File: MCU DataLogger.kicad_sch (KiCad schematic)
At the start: 25 parts, among them U1 24LC1025, U2 24LC1025, U3 DS1337S+, U4 ATMEGA328P-AU, Y1 32.768 KHz, Y2 16 MHz

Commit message: Completed comments.
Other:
- note added: "EEPROM"
- note added: "MCU"
- note added: "Mounting"
- note added: "Real time clock"
- moved on the sheet: H1, H2, H3, H4

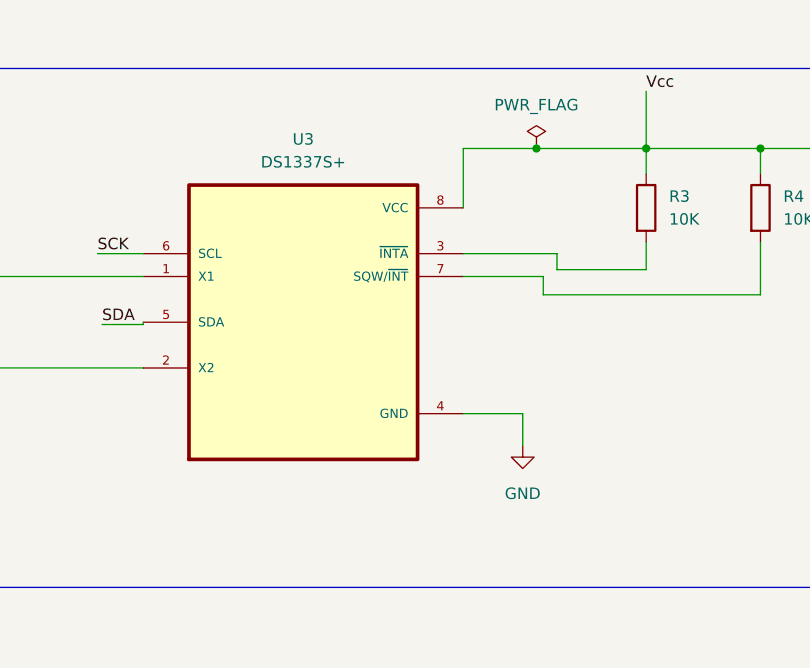
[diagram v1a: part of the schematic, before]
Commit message: First routes.
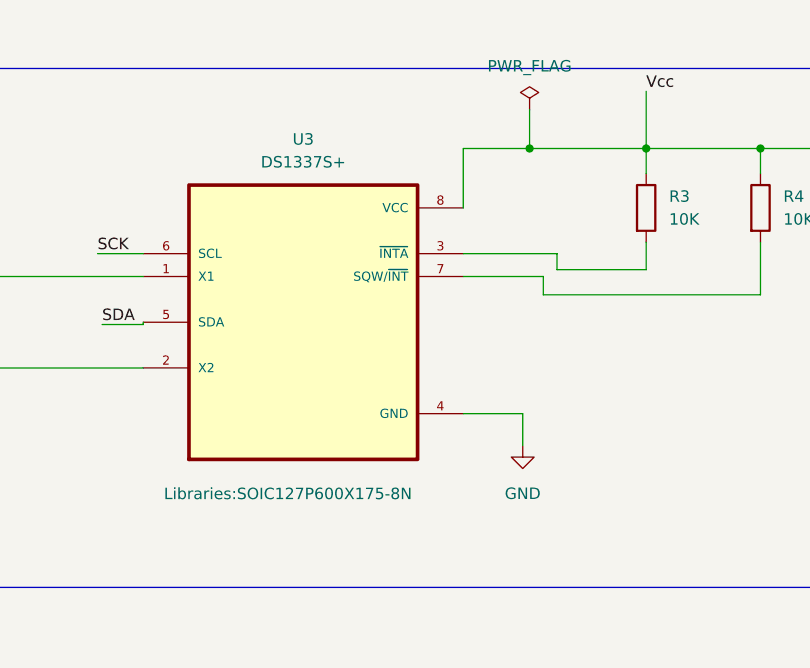
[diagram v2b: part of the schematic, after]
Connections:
- net Vcc: now also C1.1, R3.1, R4.1, U3.8 (VCC)

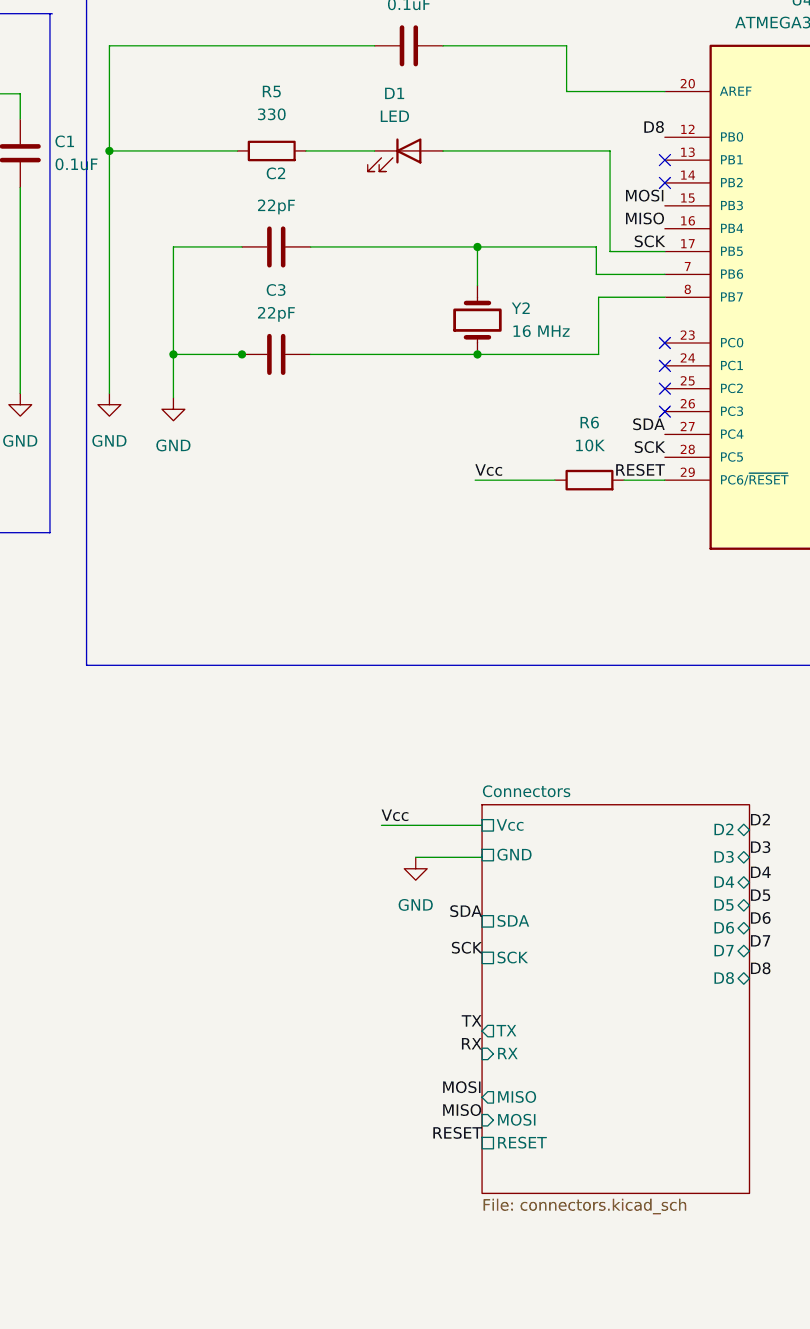
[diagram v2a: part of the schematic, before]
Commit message: Routing sans GND Vcc complete.
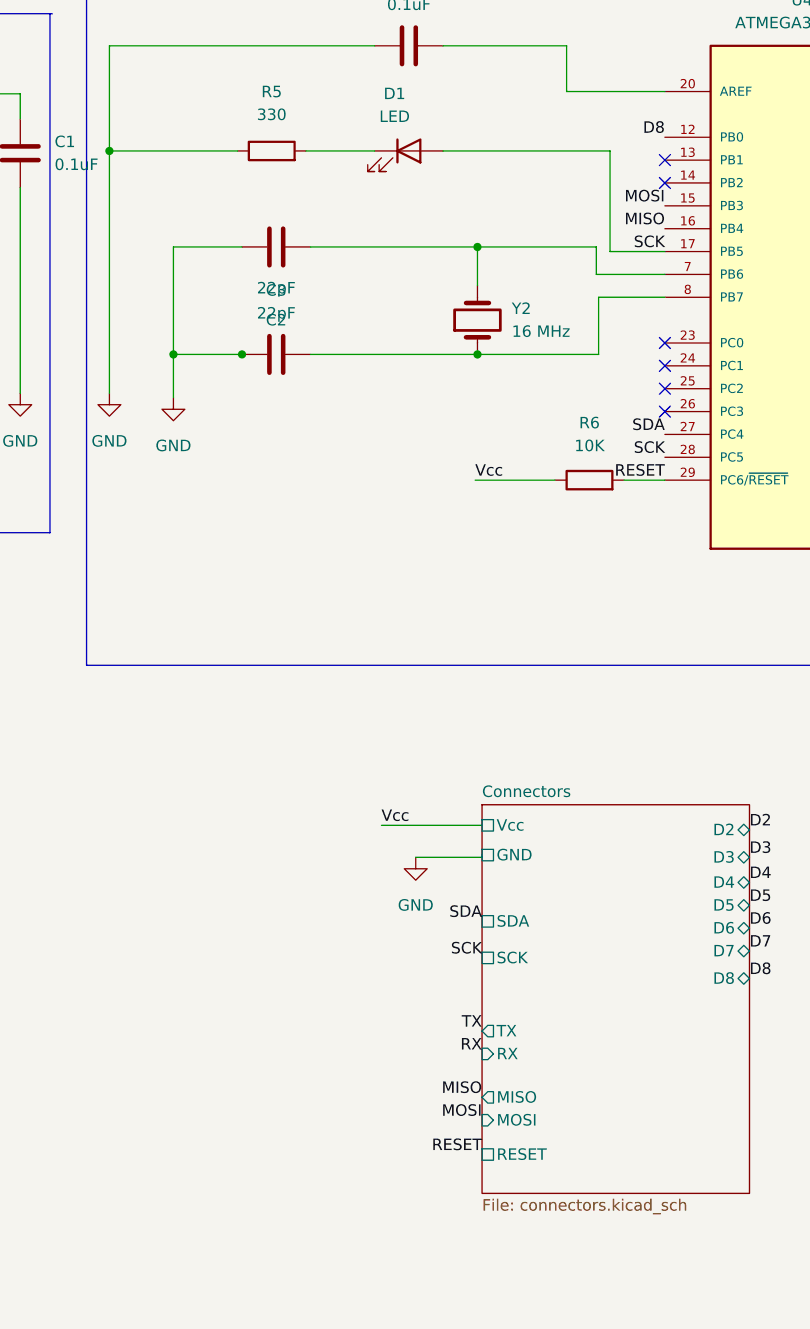
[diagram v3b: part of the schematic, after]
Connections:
- net GND: now also C2.1; no longer C2.2
- net at U4.7 (PB6), Y2.2: now also C2.2; no longer C2.1
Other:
- moved on the sheet: C2
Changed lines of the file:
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@@
     (effects (font (size 1.27 1.27)) (justify left bottom))
   )
-  (label "MISO" (at 183.388 143.002 180)
+  (label "MISO" (at 183.388 140.462 180)
     (effects (font (size 1.27 1.27)) (justify right bottom))
   )
@@
     (effects (font (size 1.27 1.27)) (justify left bottom))
   )
-  (label "RESET" (at 183.388 145.542 180)
+  (label "RESET" (at 183.388 146.812 180)
     (effects (font (size 1.27 1.27)) (justify right bottom))
   )
@@
     (effects (font (size 1.27 1.27)) (justify right bottom))
   )
-  (label "MOSI" (at 183.388 140.462 180)
+  (label "MOSI" (at 183.388 143.002 180)
     (effects (font (size 1.27 1.27)) (justify right bottom))
   )
@@
     (pin "2")
   )
-  (symbol (lib_id "Device:C") (at 160.528 45.974 270) (unit 1)
+  (symbol (lib_id "Device:C") (at 160.528 45.974 90) (unit 1)
     (in_bom yes) (on_board yes)
-    (property "Reference" "C2" (id 0) (at 160.528 37.846 90))
-    (property "Value" "22pF" (id 1) (at 160.528 41.402 90))
-    (property "Footprint" "Capacitor_SMD:C_0805_2012Metric" (id 2) (at 156.718 46.9392 0)
+    (property "Reference" "C2" (id 0) (at 160.528 54.102 90))
+    (property "Value" "22pF" (id 1) (at 160.528 50.546 90))
+    (property "Footprint" "Capacitor_SMD:C_0805_2012Metric" (id 2) (at 164.338 45.0088 0)
       (effects (font (size 1.27 1.27)) hide)
     )
@@
       (effects (font (size 1.27 1.27)) (justify left))
     )
-    (pin "RESET" passive (at 183.388 145.542 180)
-      (effects (font (size 1.27 1.27)) (justify left))
-    )
+    (pin "RESET" passive (at 183.388 146.812 180)
+      (effects (font (size 1.27 1.27)) (justify left))
+    )
